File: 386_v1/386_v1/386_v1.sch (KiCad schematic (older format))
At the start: 41 parts, among them U1 74LVC1G17GW, U10 SN74LVC4245A, U11 SN74LVC4245A, U12 74LVC1G17GW, U13 74LVC1G17GW, U2 74LVC1G17GW, U3 i386SX, U4 SN74LVC4245A, U5 SN74LVC4245A, U6 SN74LVC4245A, U7 Conn_02x32_Odd_Even, U8 Conn_02x32_Odd_Even, U9 SN74LVC4245A

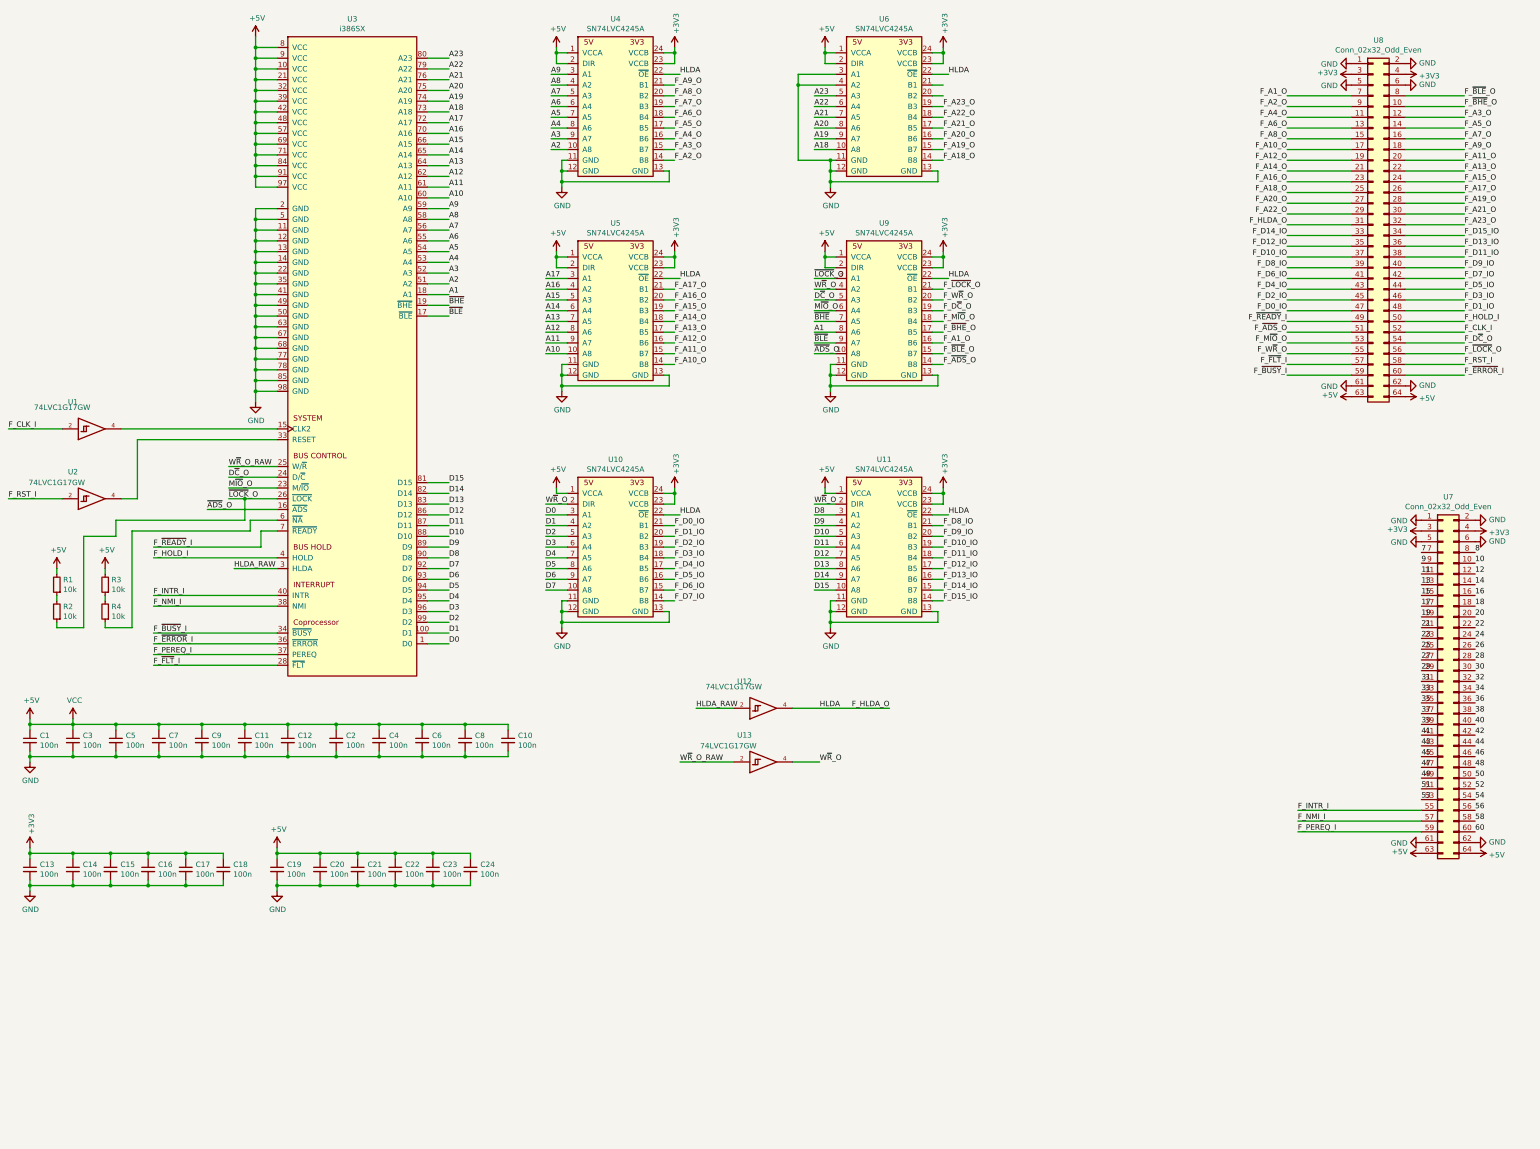
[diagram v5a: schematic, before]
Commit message: update schematic
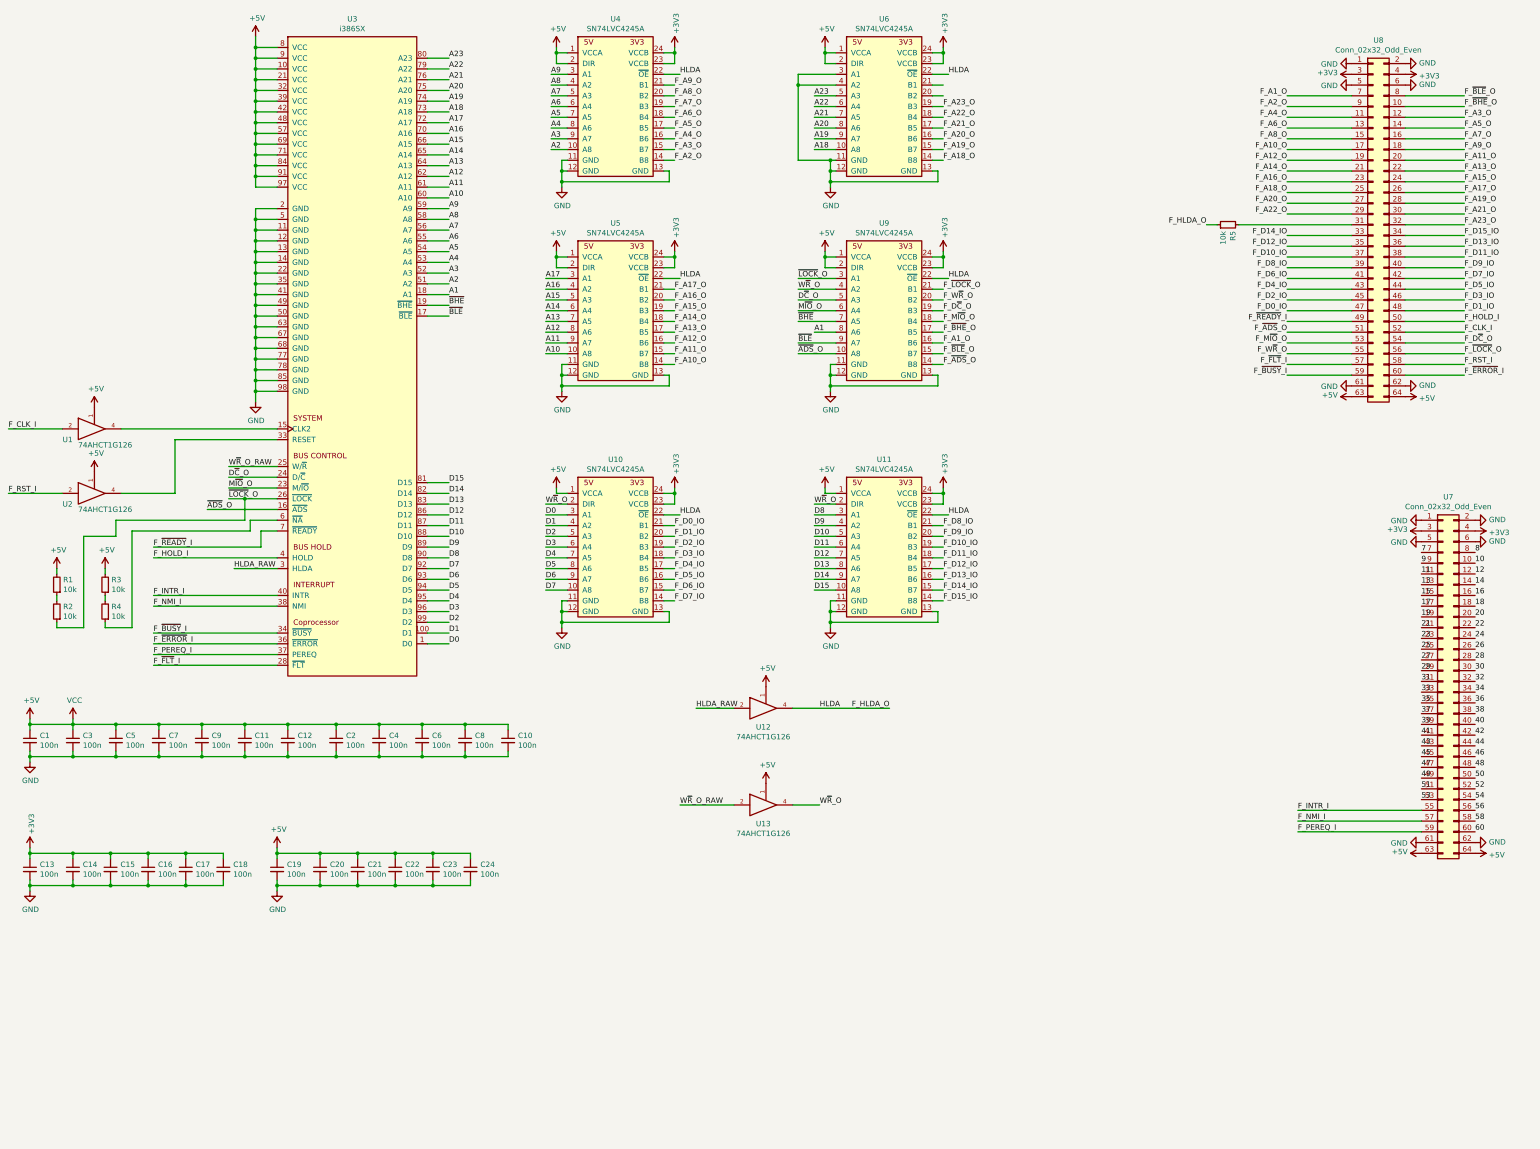
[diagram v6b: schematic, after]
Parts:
- removed U1, U12, U13, U2: 74LVC1G17GW, Package_SO:TSOP-5_1.65x3.05mm_P0.95mm, symbol 74xGxx:74LVC1G17
- added R5: 10k, Resistor_SMD:R_0805_2012Metric, symbol Device:R_Small
- added U1, U12, U13, U2: 74AHCT1G126, Package_TO_SOT_SMD:SOT-23-5, symbol 74xGxx:74AHCT1G126
- U3: footprint Package_QFP:LQFP-100_14x14mm_P0.5mm -> 386_v1:QFP-100_25x25_Pitch0.635mm
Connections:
- net +5V: now also U1.1, U1.5 (VCC), U12.1, U12.5 (VCC), U13.1, U13.5 (VCC), U2.1, U2.5 (VCC)
- net F_CLK_I: now also U1.2
- net F_HLDA_O: now also R5.1, U12.4; no longer U8.31 (Pin_31)
- net F_RST_I: now also U2.2
- net GND: now also U1.3 (GND), U12.3 (GND), U13.3 (GND), U2.3 (GND)
- net HLDA_RAW: now also U12.2
- net W~R~_O: now also U13.4
- net W~R~_O_RAW: now also U13.2
- net at U3.15 (CLK2): now also U1.4
- net at U3.33 (RESET): now also U2.4
- new net: R5.2, U8.31 (Pin_31)
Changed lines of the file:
@@
 $EndComp
 Wire Wire Line
-	3050 4550 1750 4550
+	3050 4550 2100 4550
 Wire Wire Line
 	1600 4450 3050 4450
@@
 Text Label 12550 8000 0    50   ~ 0
 F_INTR_I
-Text Label 12450 2550 2    50   ~ 0
+Text Label 11700 2550 2    50   ~ 0
 F_HLDA_O
 Text Label 14100 3450 0    50   ~ 0
@@
 Wire Wire Line
 	13050 2850 12450 2850
-Wire Wire Line
-	13050 2550 12450 2550
 Wire Wire Line
 	13050 2250 12450 2250
@@
 Text Label 9250 3250 0    50   ~ 0
 F_W~R~_O
-Text Label 550  5100 0    50   ~ 0
+Text Label 550  5050 0    50   ~ 0
 F_RST_I
-Wire Wire Line
-	550  5100 1050 5100
-Wire Wire Line
-	1750 5100 1600 5100
-Wire Wire Line
-	1750 4550 1750 5100
-$Comp
-L 74xGxx:74LVC1G17 U2
-U 1 1 5EE0FD3E
-P 1350 5100
-F 0 "U2" H 1150 4850 50  0000 C CNN
-F 1 "74LVC1G17GW" H 1000 4950 50  0000 C CNN
-F 2 "Package_SO:TSOP-5_1.65x3.05mm_P0.95mm" H 1350 5100 50  0001 C CNN
-F 3 "http://www.ti.com/lit/sg/scyt129e/scyt129e.pdf" H 1350 5100 50  0001 C CNN
-	1    1350 5100
-	1    0    0    1
-$EndComp
 Text Label 550  4450 0    50   ~ 0
 F_CLK_I
 Wire Wire Line
 	1050 4450 550  4450
-$Comp
-L 74xGxx:74LVC1G17 U1
-U 1 1 5EDDF229
-P 1350 4450
-F 0 "U1" H 1150 4200 50  0000 C CNN
-F 1 "74LVC1G17GW" H 1050 4250 50  0000 C CNN
-F 2 "Package_SO:TSOP-5_1.65x3.05mm_P0.95mm" H 1350 4450 50  0001 C CNN
-F 3 "http://www.ti.com/lit/sg/scyt129e/scyt129e.pdf" H 1350 4450 50  0001 C CNN
-	1    1350 4450
-	1    0    0    1
-$EndComp
 Wire Wire Line
 	3150 7450 3150 7500
@@
 F 0 "U3" H 3750 1165 50  0000 C CNN
 F 1 "i386SX" H 3750 1074 50  0000 C CNN
-F 2 "Package_QFP:LQFP-100_14x14mm_P0.5mm" H 3450 -2700 50  0001 C CNN
+F 2 "386_v1:QFP-100_25x25_Pitch0.635mm" H 3450 -2700 50  0001 C CNN
 F 3 "" H 3450 -2700 50  0001 C CNN
 	1    3150 900
@@
 Connection ~ 8150 2850
 Wire Wire Line
-	8050 3050 8250 3050
-Wire Wire Line
-	8050 3150 8250 3150
-Wire Wire Line
-	8250 3250 8050 3250
-Wire Wire Line
-	8050 3750 8250 3750
-Wire Wire Line
-	8250 3650 8050 3650
-Wire Wire Line
 	8050 3550 8250 3550
-Wire Wire Line
-	8050 3450 8250 3450
-Wire Wire Line
-	8250 3350 8050 3350
 Wire Wire Line
 	2600 5100 2750 5100
@@
 Wire Wire Line
 	4650 5450 4450 5450
-$Comp
-L 386_v1:SN74LVC4245A U10
-U 1 1 5FC8709F
-P 5850 5050
-F 0 "U10" H 6200 5365 50  0000 C CNN
-F 1 "SN74LVC4245A" H 6200 5274 50  0000 C CNN
-F 2 "Package_SO:TSSOP-24_4.4x7.8mm_P0.65mm" H 5850 5050 50  0001 C CNN
-F 3 "" H 5850 5050 50  0001 C CNN
-	1    5850 5050
-	1    0    0    -1
-$EndComp
 Wire Wire Line
 	5650 5050 5750 5050
@@
 Wire Wire Line
 	5550 5950 5750 5950
-Wire Wire Line
-	5750 5850 5550 5850
 Wire Wire Line
 	5550 5750 5750 5750
@@
 Wire Wire Line
 	1900 6650 3050 6650
-Text Label 8050 3150 0    50   ~ 0
+Text Label 7900 3150 0    50   ~ 0
 W~R~_O
-Text Label 8050 3250 0    50   ~ 0
+Text Label 7900 3250 0    50   ~ 0
 D~C~_O
-Text Label 8050 3350 0    50   ~ 0
+Text Label 7900 3350 0    50   ~ 0
 M~IO~_O
-Text Label 8050 3050 0    50   ~ 0
+Text Label 7900 3050 0    50   ~ 0
 ~LOCK~_O
-Text Label 8050 3750 0    50   ~ 0
+Text Label 7900 3750 0    50   ~ 0
 ~ADS~_O
 $Comp
@@
 	7900 1250 8250 1250
 Connection ~ 8200 1950
-$Comp
-L 74xGxx:74LVC1G17 U12
-U 1 1 60846793
-P 7600 7050
-F 0 "U12" H 7400 6800 50  0000 C CNN
-F 1 "74LVC1G17GW" H 7300 6850 50  0000 C CNN
-F 2 "Package_SO:TSOP-5_1.65x3.05mm_P0.95mm" H 7600 7050 50  0001 C CNN
-F 3 "http://www.ti.com/lit/sg/scyt129e/scyt129e.pdf" H 7600 7050 50  0001 C CNN
-	1    7600 7050
-	1    0    0    1
-$EndComp
-$Comp
-L 74xGxx:74LVC1G17 U13
-U 1 1 608476A8
-P 7600 7550
-F 0 "U13" H 7400 7300 50  0000 C CNN
-F 1 "74LVC1G17GW" H 7250 7400 50  0000 C CNN
-F 2 "Package_SO:TSOP-5_1.65x3.05mm_P0.95mm" H 7600 7550 50  0001 C CNN
-F 3 "http://www.ti.com/lit/sg/scyt129e/scyt129e.pdf" H 7600 7550 50  0001 C CNN
-	1    7600 7550
-	1    0    0    1
-$EndComp
 Wire Wire Line
 	7300 7050 6950 7050
@@
 Text Label 6950 7050 0    50   ~ 0
 HLDA_RAW
-Text Label 6800 7550 0    50   ~ 0
+Text Label 6800 7950 0    50   ~ 0
 W~R~_O_RAW
 Wire Wire Line
-	6800 7550 7300 7550
-Wire Wire Line
-	7850 7550 8100 7550
-Text Label 8100 7550 0    50   ~ 0
+	6800 7950 7300 7950
+Wire Wire Line
+	7850 7950 8100 7950
+Text Label 8100 7950 0    50   ~ 0
 W~R~_O
-Text Label 8050 3650 0    50   ~ 0
+Text Label 7900 3650 0    50   ~ 0
 ~BLE
 Text Label 8050 3550 0    50   ~ 0
 A1
-Text Label 8050 3450 0    50   ~ 0
+Text Label 7900 3450 0    50   ~ 0
 ~BHE
 Text Label 12450 3350 2    50   ~ 0
@@
 Wire Wire Line
 	7850 7050 8750 7050
+Wire Wire Line
+	5750 5850 5550 5850
+$Comp
+L 386_v1:SN74LVC4245A U10
+U 1 1 5FC8709F
+P 5850 5050
+F 0 "U10" H 6200 5365 50  0000 C CNN
+F 1 "SN74LVC4245A" H 6200 5274 50  0000 C CNN
+F 2 "Package_SO:TSSOP-24_4.4x7.8mm_P0.65mm" H 5850 5050 50  0001 C CNN
+F 3 "" H 5850 5050 50  0001 C CNN
+	1    5850 5050
+	1    0    0    -1
+$EndComp
+$Comp
+L 74xGxx:74AHCT1G126 U12
+U 1 1 5F519424
+P 7600 7050
+F 0 "U12" H 7575 6875 50  0000 C CNN
+F 1 "74AHCT1G126" H 7575 6784 50  0000 C CNN
+F 2 "Package_TO_SOT_SMD:SOT-23-5" H 7600 7050 50  0001 C CNN
+F 3 "http://www.ti.com/lit/sg/scyt129e/scyt129e.pdf" H 7600 7050 50  0001 C CNN
+	1    7600 7050
+	1    0    0    -1
+$EndComp
+$Comp
+L 74xGxx:74AHCT1G126 U1
+U 1 1 5F569CED
+P 1350 4450
+F 0 "U1" H 1100 4350 50  0000 C CNN
+F 1 "74AHCT1G126" H 1450 4300 50  0000 C CNN
+F 2 "Package_TO_SOT_SMD:SOT-23-5" H 1350 4450 50  0001 C CNN
+F 3 "http://www.ti.com/lit/sg/scyt129e/scyt129e.pdf" H 1350 4450 50  0001 C CNN
+	1    1350 4450
+	1    0    0    -1
+$EndComp
+$Comp
+L 74xGxx:74AHCT1G126 U2
+U 1 1 5F56ADC8
+P 1350 5050
+F 0 "U2" H 1100 4950 50  0000 C CNN
+F 1 "74AHCT1G126" H 1450 4900 50  0000 C CNN
+F 2 "Package_TO_SOT_SMD:SOT-23-5" H 1350 5050 50  0001 C CNN
+F 3 "http://www.ti.com/lit/sg/scyt129e/scyt129e.pdf" H 1350 5050 50  0001 C CNN
+	1    1350 5050
+	1    0    0    -1
+$EndComp
+Wire Wire Line
+	550  5050 1050 5050
+Wire Wire Line
+	1600 5050 2100 5050
+Wire Wire Line
+	2100 5050 2100 4550
+$Comp
+L power:+5V #PWR04
+U 1 1 5F7471E8
+P 1350 4850
+F 0 "#PWR04" H 1350 4700 50  0001 C CNN
+F 1 "+5V" H 1365 5023 50  0000 C CNN
+F 2 "" H 1350 4850 50  0001 C CNN
+F 3 "" H 1350 4850 50  0001 C CNN
+	1    1350 4850
+	1    0    0    -1
+$EndComp
+$Comp
+L power:+5V #PWR03
+U 1 1 5F7476EF
+P 1350 4250
+F 0 "#PWR03" H 1350 4100 50  0001 C CNN
+F 1 "+5V" H 1365 4423 50  0000 C CNN
+F 2 "" H 1350 4250 50  0001 C CNN
+F 3 "" H 1350 4250 50  0001 C CNN
+	1    1350 4250
+	1    0    0    -1
+$EndComp
+$Comp
+L 74xGxx:74AHCT1G126 U13
+U 1 1 5F747B2F
+P 7600 7950
+F 0 "U13" H 7575 7775 50  0000 C CNN
+F 1 "74AHCT1G126" H 7575 7684 50  0000 C CNN
+F 2 "Package_TO_SOT_SMD:SOT-23-5" H 7600 7950 50  0001 C CNN
+F 3 "http://www.ti.com/lit/sg/scyt129e/scyt129e.pdf" H 7600 7950 50  0001 C CNN
+	1    7600 7950
+	1    0    0    -1
+$EndComp
+$Comp
+L power:+5V #PWR06
+U 1 1 5F748E92
+P 7600 7750
+F 0 "#PWR06" H 7600 7600 50  0001 C CNN
+F 1 "+5V" H 7615 7923 50  0000 C CNN
+F 2 "" H 7600 7750 50  0001 C CNN
+F 3 "" H 7600 7750 50  0001 C CNN
+	1    7600 7750
+	1    0    0    -1
+$EndComp
+$Comp
+L power:+5V #PWR0136
+U 1 1 5F83FE32
+P 7600 6850
+F 0 "#PWR0136" H 7600 6700 50  0001 C CNN
+F 1 "+5V" H 7615 7023 50  0000 C CNN
+F 2 "" H 7600 6850 50  0001 C CNN
+F 3 "" H 7600 6850 50  0001 C CNN
+	1    7600 6850
+	1    0    0    -1
+$EndComp
+$Comp
+L Device:R_Small R5
+U 1 1 5F5C13F1
+P 11900 2550
+F 0 "R5" H 11841 2504 50  0000 R CNN
+F 1 "10k" H 11841 2595 50  0000 R CNN
+F 2 "Resistor_SMD:R_0805_2012Metric" H 11900 2550 50  0001 C CNN
+F 3 "~" H 11900 2550 50  0001 C CNN
+	1    11900 2550
+	0    -1   -1   0
+$EndComp
+Wire Wire Line
+	11700 2550 11800 2550
+Wire Wire Line
+	12000 2550 13050 2550
+Wire Wire Line
+	7900 3750 8250 3750
+Wire Wire Line
+	7900 3650 8250 3650
+Wire Wire Line
+	7900 3450 8250 3450
+Wire Wire Line
+	7900 3350 8250 3350
+Wire Wire Line
+	7900 3250 8250 3250
+Wire Wire Line
+	7900 3150 8250 3150
+Wire Wire Line
+	7900 3050 8250 3050
 $EndSCHEMATC
